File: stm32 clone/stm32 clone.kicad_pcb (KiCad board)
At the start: 2 copper layers, 10 parts, among them U1 STM32G030C6T6, Y1 8 MHz, Y2 32.768 KHz

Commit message: pcb init and bill
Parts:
- added C10: 100nF, Capacitor_SMD:C_0805_2012Metric_Pad1.18x1.45mm_HandSolder, F.Cu at (103.3, 61.1)
- added C11: 10uF, Capacitor_SMD:C_0805_2012Metric_Pad1.18x1.45mm_HandSolder, F.Cu at (103.3, 64.1)
- added C12: 10uF, Capacitor_SMD:C_0805_2012Metric_Pad1.18x1.45mm_HandSolder, F.Cu at (103.3, 67.1)
- added C13: 10nF, Capacitor_SMD:C_0805_2012Metric_Pad1.18x1.45mm_HandSolder, F.Cu at (103.3, 70.1)
- added C8: 0.1uF, Capacitor_SMD:C_0805_2012Metric_Pad1.18x1.45mm_HandSolder, F.Cu at (103.3, 55.1)
- added C9: 10uF, Capacitor_SMD:C_0805_2012Metric_Pad1.18x1.45mm_HandSolder, F.Cu at (103.3, 58.1)
- added D1: 1N5819, Diode_THT:D_DO-15_P12.70mm_Horizontal, F.Cu at (107.7, 73.2)
- added D2: 1N5908, Diode_THT:D_DO-201AE_P15.24mm_Horizontal, F.Cu at (102.9, 50.1)
- added D3: LED_PWR, LED_THT:LED_D5.0mm, F.Cu at (118.7, 57.3)
- added D4: LED, LED_THT:LED_D5.0mm, F.Cu at (118.7, 64.8)
- added J1: DEBUG, Connector_PinHeader_2.54mm:PinHeader_1x05_P2.54mm_Vertical, F.Cu at (98.6, 76.4)
- added J2: USB_C_Receptacle_USB2.0_16P, Connector_USB:USB_C_Receptacle_GCT_USB4105-xx-A_16P_TopMnt_Horizontal, F.Cu at (111.5, 81.1)
- added J3: PA-PC-PB-Conn, Connector_PinHeader_2.54mm:PinHeader_1x10_P2.54mm_Vertical, F.Cu at (98.6, 49.0)
- added J5: PB-PD-Conn, Connector_PinHeader_2.54mm:PinHeader_1x12_P2.54mm_Vertical, F.Cu at (89.4, 49.0)
- added J6: PA-Conn, Connector_PinHeader_2.54mm:PinHeader_1x02_P2.54mm_Vertical, F.Cu at (94.0, 79.0)
- added J7: PA-PB-Conn, Connector_PinHeader_2.54mm:PinHeader_1x11_P2.54mm_Vertical, F.Cu at (94.0, 49.0)
- added R1: 5k1, Resistor_SMD:R_0805_2012Metric_Pad1.20x1.40mm_HandSolder, F.Cu at (103.2, 73.1)
- added R2: 5k1, Resistor_SMD:R_0805_2012Metric_Pad1.20x1.40mm_HandSolder, F.Cu at (103.2, 76.0)
- added R3: 1k, Resistor_SMD:R_0805_2012Metric_Pad1.20x1.40mm_HandSolder, F.Cu at (103.2, 79.0)
- added R4: 1k, Resistor_SMD:R_0805_2012Metric_Pad1.20x1.40mm_HandSolder, F.Cu at (103.2, 81.9)
- added R5: 1k, Resistor_SMD:R_0805_2012Metric_Pad1.20x1.40mm_HandSolder, F.Cu at (103.2, 84.9)
- added R6: 10k, Resistor_SMD:R_0805_2012Metric_Pad1.20x1.40mm_HandSolder, F.Cu at (103.2, 87.8)
- added SW1: RST, Button_Switch_THT:SW_PUSH_6mm_2pin, F.Cu at (111.0, 57.8)
- added SW2: USR_BTN, Button_Switch_THT:SW_PUSH_6mm_2pin, F.Cu at (111.0, 66.4)
- added U2: TPS1117LV33S, Package_TO_SOT_SMD:SOT-223-3_TabPin2, F.Cu at (122.3, 80.0)
- C1, C3: value 100n -> 100nF
- C2: value 4.7u -> 4.7uF
- C4, C5: value 22p -> 22pF
- C6, C7: value 18p -> 18pF
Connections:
- U1 pad 1: unconnected-(U1-PC13-Pad1) -> /PC13-USR_BTN
- U1 pad 10: unconnected-(U1-NRST-Pad10) -> /NRST
- U1 pad 11: unconnected-(U1-PA0-Pad11) -> /PA0
- U1 pad 12: unconnected-(U1-PA1-Pad12) -> /PA1
- U1 pad 13: unconnected-(U1-PA2-Pad13) -> /PA2
- U1 pad 14: unconnected-(U1-PA3-Pad14) -> /PA3
- U1 pad 15: unconnected-(U1-PA4-Pad15) -> /PA4
- U1 pad 16: unconnected-(U1-PA5-Pad16) -> /PA5-USR_LED
- U1 pad 17: unconnected-(U1-PA6-Pad17) -> /PA6
- U1 pad 18: unconnected-(U1-PA7-Pad18) -> /PA7
- U1 pad 19: unconnected-(U1-PB0-Pad19) -> /PB0
- U1 pad 20: unconnected-(U1-PB1-Pad20) -> /PB1
- U1 pad 21: unconnected-(U1-PB2-Pad21) -> /PB2
- U1 pad 22: unconnected-(U1-PB10-Pad22) -> /PB10
- U1 pad 23: unconnected-(U1-PB11-Pad23) -> /PB11
- U1 pad 24: unconnected-(U1-PB12-Pad24) -> /PB12
- U1 pad 25: unconnected-(U1-PB13-Pad25) -> /PB13
- U1 pad 26: unconnected-(U1-PB14-Pad26) -> /PB14
- U1 pad 27: unconnected-(U1-PB15-Pad27) -> /PB15
- U1 pad 28: unconnected-(U1-PA8-Pad28) -> /PA8
- U1 pad 29: unconnected-(U1-NC/PA9-Pad29) -> /PA9
- U1 pad 30: unconnected-(U1-PC6-Pad30) -> /PC6
- U1 pad 31: unconnected-(U1-PC7-Pad31) -> /PC7
- U1 pad 32: unconnected-(U1-NC/PA10-Pad32) -> /PA10
- U1 pad 33: unconnected-(U1-PA9/PA11-Pad33) -> /PA11
- U1 pad 34: unconnected-(U1-PA10/PA12-Pad34) -> /PA12
- U1 pad 35: unconnected-(U1-PA13-Pad35) -> /SWDIO
- U1 pad 36: unconnected-(U1-PA14-Pad36) -> /SWCLK
- U1 pad 37: unconnected-(U1-PA15-Pad37) -> /PA15
- U1 pad 38: unconnected-(U1-PD0-Pad38) -> /PD0
- U1 pad 39: unconnected-(U1-PD1-Pad39) -> /PD1
- U1 pad 40: unconnected-(U1-PD2-Pad40) -> /PD2
- U1 pad 41: unconnected-(U1-PD3-Pad41) -> /PD3
- U1 pad 42: unconnected-(U1-PB3-Pad42) -> /PB3
- U1 pad 43: unconnected-(U1-PB4-Pad43) -> /PB4
- U1 pad 44: unconnected-(U1-PB5-Pad44) -> /PB5
- U1 pad 45: unconnected-(U1-PB6-Pad45) -> /PB6
- U1 pad 46: unconnected-(U1-PB7-Pad46) -> /PB7
- U1 pad 47: unconnected-(U1-PB8-Pad47) -> /PB8
- U1 pad 48: unconnected-(U1-PB9-Pad48) -> /PB9
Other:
- copper layers 2 -> 4

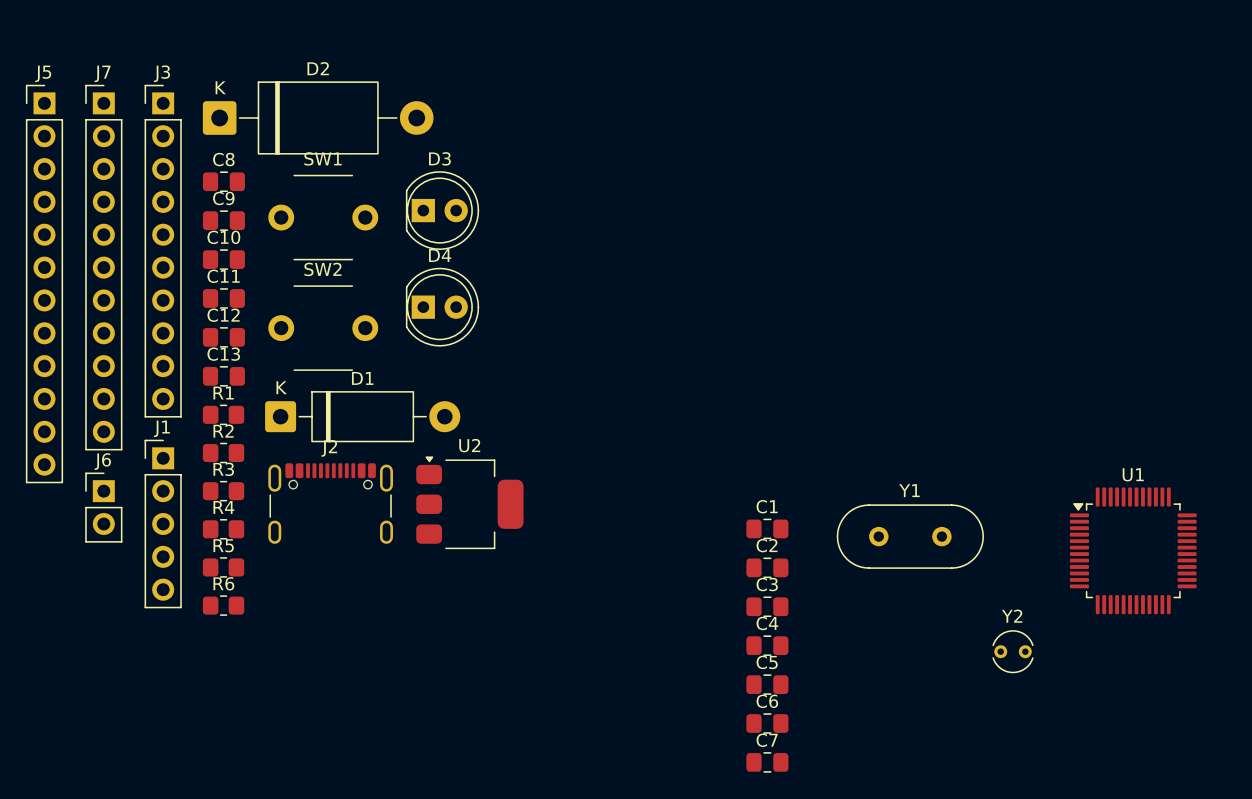
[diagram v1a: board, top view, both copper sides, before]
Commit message: component placement, main routes
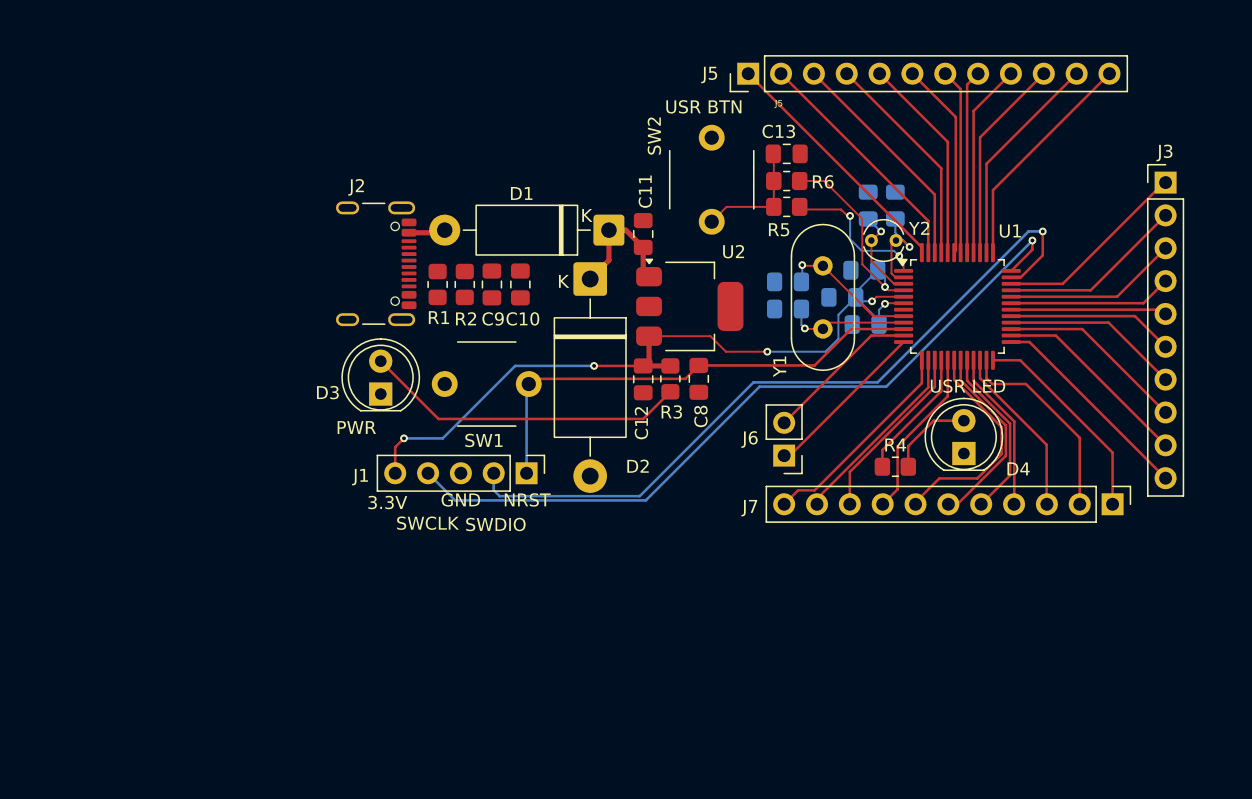
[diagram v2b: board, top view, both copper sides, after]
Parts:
- C1, C2, C3, C4, C5, C6, C7: moved to B.Cu
- moved J7 84.0 mm to (172.0, 80.0), turned to -90 degrees
- moved J3 77.8 mm to (176.1, 55.1)
- moved R6 54.5 mm to (146.8, 55.0), turned to 180 degrees
- moved J5 54.5 mm to (143.8, 46.7), turned to 90 degrees
- moved J6 52.7 mm to (146.6, 76.2), turned to 180 degrees
- moved R4 52.2 mm to (155.2, 77.1)
- moved R5 51.7 mm to (146.8, 57.0), turned to 180 degrees
- moved C13 46.8 mm to (146.8, 52.9)
- moved C7 43.8 mm to (153.1, 56.9), turned to -90 degrees
- moved D4 43.3 mm to (160.5, 76.1), turned to 90 degrees
- moved C6 41.3 mm to (155.2, 56.9), turned to -90 degrees
- moved C8 39.8 mm to (140.0, 70.3), turned to -90 degrees
- moved R3 35.6 mm to (137.8, 70.3), turned to -90 degrees
- moved Y2 33.3 mm to (153.3, 59.6)
- moved C11 32.8 mm to (135.7, 59.1), turned to 90 degrees
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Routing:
- net +3.3V: track 0.00 -> 75.7 mm, vias 0 -> 6
- net /SWCLK: track 0.00 -> 59.0 mm, vias 0 -> 1
- net /SWDIO: track 0.00 -> 57.4 mm, vias 0 -> 1
- net /NRST: track 0.00 -> 37.7 mm
- net Net-(D3-A): track 0.00 -> 25.1 mm
- net /PB9: track 0.00 -> 19.4 mm
- net /PB8: track 0.00 -> 18.6 mm
- net /PB7: track 0.00 -> 17.7 mm
- net /PA15: track 0.00 -> 17.6 mm
- net /PA7: track 0.00 -> 17.1 mm
- net /PB6: track 0.00 -> 16.9 mm
- net /PD0: track 0.00 -> 16.7 mm
- net /PA2: track 0.00 -> 16.3 mm
- net /PB13: track 0.00 -> 16.3 mm
- net /PB12: track 0.00 -> 16.2 mm
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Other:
- board text added: "3.3V"
- board text added: "GND"
- board text added: "J5"
- board text added: "NRST"
- board text added: "PWR"
- board text added: "SWCLK"
- board text added: "SWDIO"
- board text added: "USR BTN"
- board text added: "USR LED"

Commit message: connections, edge cuts
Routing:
- net +5V: track 10.0 -> 17.9 mm
- net Net-(J2-CC1): track 0.00 -> 5.08 mm
- net Net-(J2-CC2): track 0.00 -> 2.69 mm
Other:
- board outline added: 67.3 x 39.8 mm
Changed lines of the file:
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@@
 		(tags "LED")
 		(property "Reference" "D3"
-			(at 0.075 -4.1 180)
+			(at -2.925 -2.7 180)
 			(layer "F.SilkS")
 			(effects
@@
 		)
 	)
+	(gr_rect
+		(start 111.4 43.7)
+		(end 178.7 83.5)
+		(stroke
+			(width 0.05)
+			(type default)
+		)
+		(fill no)
+		(layer "Edge.Cuts")
+	)
 	(gr_text "J5"
 		(at 146.2 49 0)
@@
 	)
 	(gr_text "PWR"
-		(at 113.5 74.1 0)
+		(at 115.7 74.4 0)
 		(layer "F.SilkS")
 		(effects
@@
 		)
 	)
+	(dimension
+		(type orthogonal)
+		(layer "Edge.Cuts")
+		(pts
+			(xy 111.4 43.7) (xy 178.7 43.7)
+		)
+		(height -9.8)
+		(orientation 0)
+		(format
+			(prefix "")
+			(suffix "")
+			(units 3)
+			(units_format 0)
+			(precision 4)
+			(suppress_zeroes yes)
+		)
+		(style
+			(thickness 0.05)
+			(arrow_length 1.27)
+			(text_position_mode 0)
+			(arrow_direction outward)
+			(extension_height 0.58642)
+			(extension_offset 0.5)
+			(keep_text_aligned yes)
+		)
+		(gr_text "67,3"
+			(at 145.05 32.75 0)
+			(layer "Edge.Cuts")
+			(effects
+				(font
+					(size 1 1)
+					(thickness 0.15)
+				)
+			)
+		)
+	)
+	(dimension
+		(type orthogonal)
+		(layer "Edge.Cuts")
+		(pts
+			(xy 178.7 43.7) (xy 178.7 83.5)
+		)
+		(height 15.8)
+		(orientation 1)
+		(format
+			(prefix "")
+			(suffix "")
+			(units 3)
+			(units_format 0)
+			(precision 4)
+			(suppress_zeroes yes)
+		)
+		(style
+			(thickness 0.05)
+			(arrow_length 1.27)
+			(text_position_mode 0)
+			(arrow_direction outward)
+			(extension_height 0.58642)
+			(extension_offset 0.5)
+			(keep_text_aligned yes)
+		)
+		(gr_text "39,8"
+			(at 193.35 63.6 90)
+			(layer "Edge.Cuts")
+			(effects
+				(font
+					(size 1 1)
+					(thickness 0.15)
+				)
+			)
+		)
+	)
 	(segment
 		(start 127.25 70.3)
@@
 	)
 	(segment
-		(start 149.6 66.44)
-		(end 148.24 66.44)
-		(width 0.15)
+		(start 121.9 62)
+		(end 121.4 62)
+		(width 0.2)
 		(layer "F.Cu")
-		(net "/OSC_OUT")
+		(net "Net-(J2-CC1)")
 	)
 	(segment
-		(start 150.09 65.95)
-		(end 149.6 66.44)
-		(width 0.15)
+		(start 121.4 62)
+		(end 119.55 60.15)
+		(width 0.2)
 		(layer "F.Cu")
-		(net "/OSC_OUT")
+		(net "Net-(J2-CC1)")
 	)
 	(segment
-		(start 148.24 66.44)
-		(end 148.2 66.4)
-		(width 0.15)
+		(start 119.55 60.15)
+		(end 117.59 60.15)
+		(width 0.2)
 		(layer "F.Cu")
-		(net "/OSC_OUT")
+		(net "Net-(J2-CC1)")
 	)
 	(segment
-		(start 155.8375 65.95)
-		(end 150.09 65.95)
-		(width 0.15)
+		(start 119.8 62)
+		(end 118.65 63.15)
+		(width 0.2)
 		(layer "F.Cu")
-		(net "/OSC_OUT")
-	)
-	(via
-		(at 148.2 66.4)
-		(size 0.6)
-		(drill 0.3)
-		(layers "F.Cu" "B.Cu")
-		(net "/OSC_OUT")
+		(net "Net-(J2-CC2)")
 	)
 	(segment
-		(start 147.9375 66.1375)
-		(end 147.9375 64.9)
-		(width 0.15)
-		(layer "B.Cu")
-		(net "/OSC_OUT")
-	)
-	(segment
-		(start 148.2 66.4)
-		(end 147.9375 66.1375)
-		(width 0.15)
-		(layer "B.Cu")
-		(net "/OSC_OUT")
+		(start 118.65 63.15)
+		(end 117.59 63.15)
+		(width 0.2)
+		(layer "F.Cu")
+		(net "Net-(J2-CC2)")
 	)
 	(segment
@@
 	)
 	(segment
-		(start 155.25 59.6)
-		(end 155.8 59.6)
-		(width 0.15)
-		(layer "F.Cu")
-		(net "/OSC32_IN")
-	)
-	(segment
-		(start 155.8 59.6)
-		(end 156.3 60.1)
-		(width 0.15)
-		(layer "F.Cu")
-		(net "/OSC32_IN")
-	)
-	(segment
-		(start 155.206184 62.45)
-		(end 154.898 62.141816)
-		(width 0.15)
-		(layer "F.Cu")
-		(net "/OSC32_IN")
-	)
-	(segment
-		(start 154.898 62.141816)
-		(end 154.898 59.952)
-		(width 0.15)
+		(start 133.05 58.8)
+		(end 133.05 61.13)
+		(width 0.4)
 		(layer "F.Cu")
-		(net "/OSC32_IN")
+		(net "+5V")
 	)
 	(segment
-		(start 155.8375 62.45)
-		(end 155.206184 62.45)
-		(width 0.15)
+		(start 131.6 62.58)
+		(end 129.28 62.58)
+		(width 0.4)
 		(layer "F.Cu")
-		(net "/OSC32_IN")
+		(net "+5V")
 	)
 	(segment
-		(start 154.898 59.952)
-		(end 155.25 59.6)
-		(width 0.15)
+		(start 135.7 61.95)
+		(end 136.15 62.4)
+		(width 0.4)
 		(layer "F.Cu")
-		(net "/OSC32_IN")
-	)
-	(via
-		(at 156.3 60.1)
-		(size 0.6)
-		(drill 0.3)
-		(layers "F.Cu" "B.Cu")
-		(net "/OSC32_IN")
-	)
-	(segment
-		(start 155.2 59)
-		(end 155.2 57.9375)
-		(width 0.15)
-		(layer "B.Cu")
-		(net "/OSC32_IN")
-	)
-	(segment
-		(start 156.3 60.1)
-		(end 155.2 59)
-		(width 0.15)
-		(layer "B.Cu")
-		(net "/OSC32_IN")
+		(net "+5V")
 	)
 	(segment
-		(start 133.05 58.8)
-		(end 133.05 61.13)
+		(start 126.2 61.9625)
+		(end 124 61.9625)
 		(width 0.4)
 		(layer "F.Cu")
@@
 	)
 	(segment
-		(start 135.7 61.95)
-		(end 136.15 62.4)
+		(start 128.6625 61.9625)
+		(end 126.2 61.9625)
 		(width 0.4)
 		(layer "F.Cu")
@@
 	)
 	(segment
+		(start 129.28 62.58)
+		(end 128.6625 61.9625)
+		(width 0.4)
+		(layer "F.Cu")
+		(net "+5V")
+	)
+	(segment
 		(start 133.05 61.13)
 		(end 131.6 62.58)
@@
 	)
 	(segment
+		(start 135.7 73.4)
+		(end 119.865 73.4)
+		(width 0.2)
+		(layer "F.Cu")
+		(net "Net-(D3-A)")
+	)
+	(segment
+		(start 119.865 73.4)
+		(end 115.4 68.935)
+		(width 0.2)
+		(layer "F.Cu")
+		(net "Net-(D3-A)")
+	)
+	(segment
+		(start 137.8 71.3)
+		(end 135.7 73.4)
+		(width 0.2)
+		(layer "F.Cu")
+		(net "Net-(D3-A)")
+	)
+	(segment
+		(start 149.6 66.44)
+		(end 148.24 66.44)
+		(width 0.15)
+		(layer "F.Cu")
+		(net "/OSC_OUT")
+	)
+	(segment
+		(start 150.09 65.95)
+		(end 149.6 66.44)
+		(width 0.15)
+		(layer "F.Cu")
+		(net "/OSC_OUT")
+	)
+	(segment
+		(start 148.24 66.44)
+		(end 148.2 66.4)
+		(width 0.15)
+		(layer "F.Cu")
+		(net "/OSC_OUT")
+	)
+	(segment
+		(start 155.8375 65.95)
+		(end 150.09 65.95)
+		(width 0.15)
+		(layer "F.Cu")
+		(net "/OSC_OUT")
+	)
+	(via
+		(at 148.2 66.4)
+		(size 0.6)
+		(drill 0.3)
+		(layers "F.Cu" "B.Cu")
+		(net "/OSC_OUT")
+	)
+	(segment
+		(start 147.9375 66.1375)
+		(end 147.9375 64.9)
+		(width 0.15)
+		(layer "B.Cu")
+		(net "/OSC_OUT")
+	)
+	(segment
+		(start 148.2 66.4)
+		(end 147.9375 66.1375)
+		(width 0.15)
+		(layer "B.Cu")
+		(net "/OSC_OUT")
+	)
+	(segment
 		(start 148.06 61.56)
 		(end 148 61.5)
@@
 	)
 	(segment
-		(start 135.7 73.4)
-		(end 119.865 73.4)
-		(width 0.2)
+		(start 155.25 59.6)
+		(end 155.8 59.6)
+		(width 0.15)
 		(layer "F.Cu")
-		(net "Net-(D3-A)")
+		(net "/OSC32_IN")
 	)
 	(segment
-		(start 119.865 73.4)
-		(end 115.4 68.935)
-		(width 0.2)
+		(start 155.8 59.6)
+		(end 156.3 60.1)
+		(width 0.15)
 		(layer "F.Cu")
-		(net "Net-(D3-A)")
+		(net "/OSC32_IN")
 	)
 	(segment
-		(start 137.8 71.3)
-		(end 135.7 73.4)
-		(width 0.2)
+		(start 155.206184 62.45)
+		(end 154.898 62.141816)
+		(width 0.15)
 		(layer "F.Cu")
-		(net "Net-(D3-A)")
+		(net "/OSC32_IN")
+	)
+	(segment
+		(start 154.898 62.141816)
+		(end 154.898 59.952)
+		(width 0.15)
+		(layer "F.Cu")
+		(net "/OSC32_IN")
+	)
+	(segment
+		(start 155.8375 62.45)
+		(end 155.206184 62.45)
+		(width 0.15)
+		(layer "F.Cu")
+		(net "/OSC32_IN")
+	)
+	(segment
+		(start 154.898 59.952)
+		(end 155.25 59.6)
+		(width 0.15)
+		(layer "F.Cu")
+		(net "/OSC32_IN")
+	)
+	(via
+		(at 156.3 60.1)
+		(size 0.6)
+		(drill 0.3)
+		(layers "F.Cu" "B.Cu")
+		(net "/OSC32_IN")
+	)
+	(segment
+		(start 155.2 59)
+		(end 155.2 57.9375)
+		(width 0.15)
+		(layer "B.Cu")
+		(net "/OSC32_IN")
+	)
+	(segment
+		(start 156.3 60.1)
+		(end 155.2 59)
+		(width 0.15)
+		(layer "B.Cu")
+		(net "/OSC32_IN")
 	)
 	(segment

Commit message: gnd, connections, drc rules
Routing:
- net GND: track 0.00 -> 25.8 mm
- net Net-(D1-A): track 2.84 -> 9.43 mm
- added copper zone on B.Cu, net GND
- added copper zone on F.Cu, net GND
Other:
- board size 67.3 x 39.8 mm -> 67.4 x 38.4 mm

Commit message: fin i think
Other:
- board text added: "15.10.2026 MS STM32 Clone Function over form"
- board text added: "PA10"
- board text added: "PA11"
- board text added: "PA12"
- board text added: "PA15"
- board text added: "PA2"
- board text added: "PA3"
- board text added: "PA4"
- board text added: "PA6"
- board text added: "PA7"
- board text added: "PA8"
- board text added: "PA9"
- board text added: "PB0"
- board text added: "PB1"
- board text added: "PB10"
- board text added: "PB11"
- board text added: "PB12"
- board text added: "PB13"
- board text added: "PB14"
- board text added: "PB15"
- board text added: "PB2"
- board text added: "PB3"
- board text added: "PB4"
- board text added: "PB5"
- board text added: "PB6"
- board text added: "PB7"
- board text added: "PB8"
- board text added: "PB9"
- board text added: "PC6"
- board text added: "PC7"
- board text added: "PD0"
- board text added: "PD1"
- board text added: "PD2"
- board text added: "PD3"
- board text removed: "J5"
